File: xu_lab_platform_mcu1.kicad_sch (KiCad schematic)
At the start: 1 part, among them U1 STM32F446RCTx

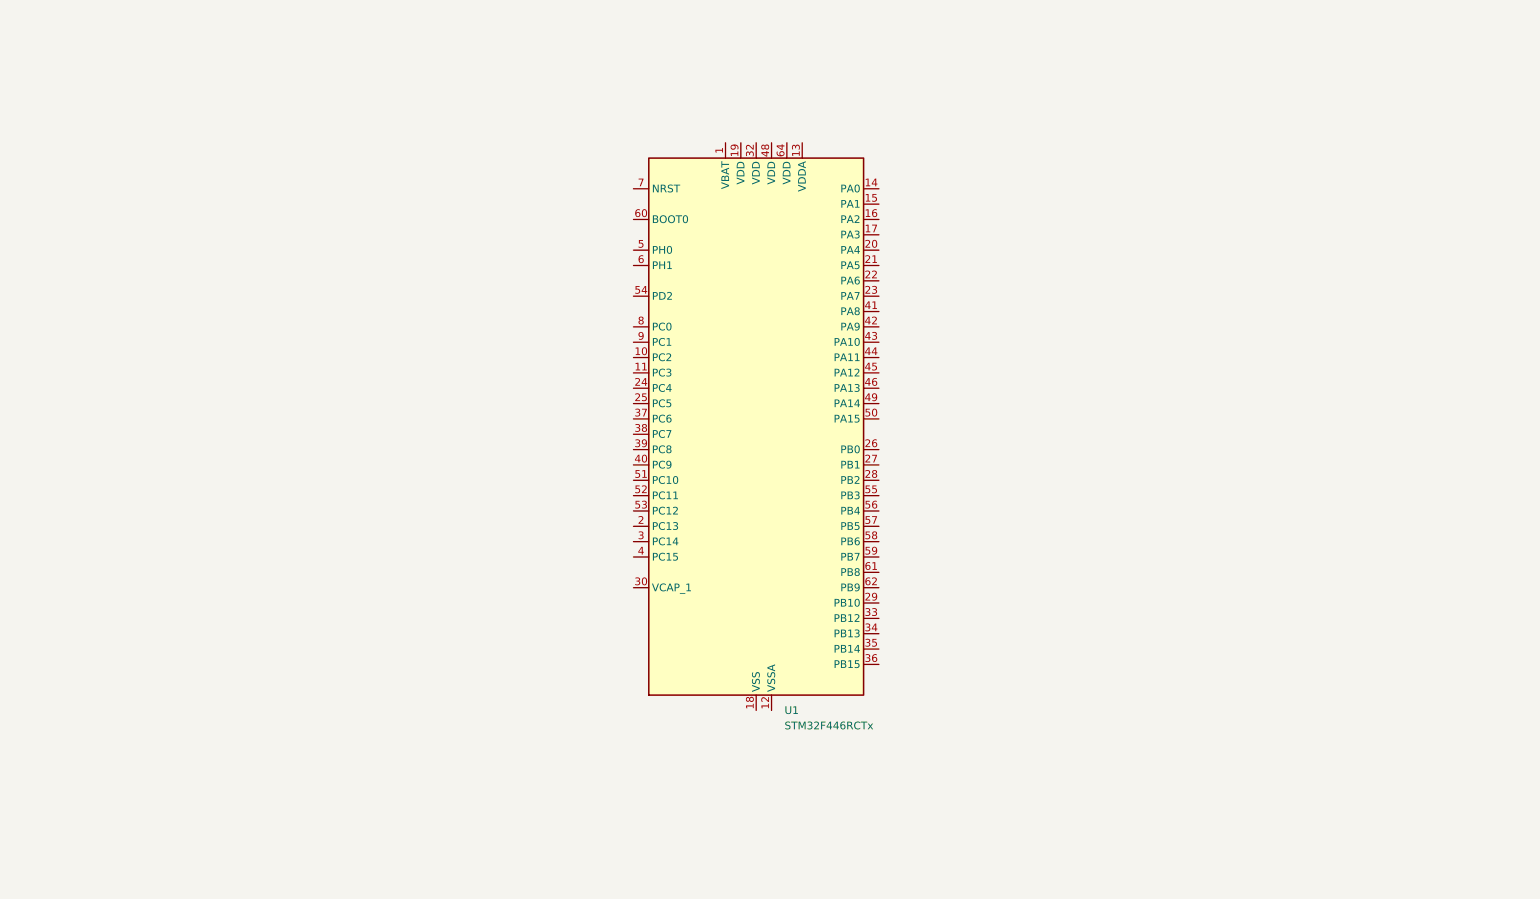
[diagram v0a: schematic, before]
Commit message: Connect power pins and add decoupling capacitors
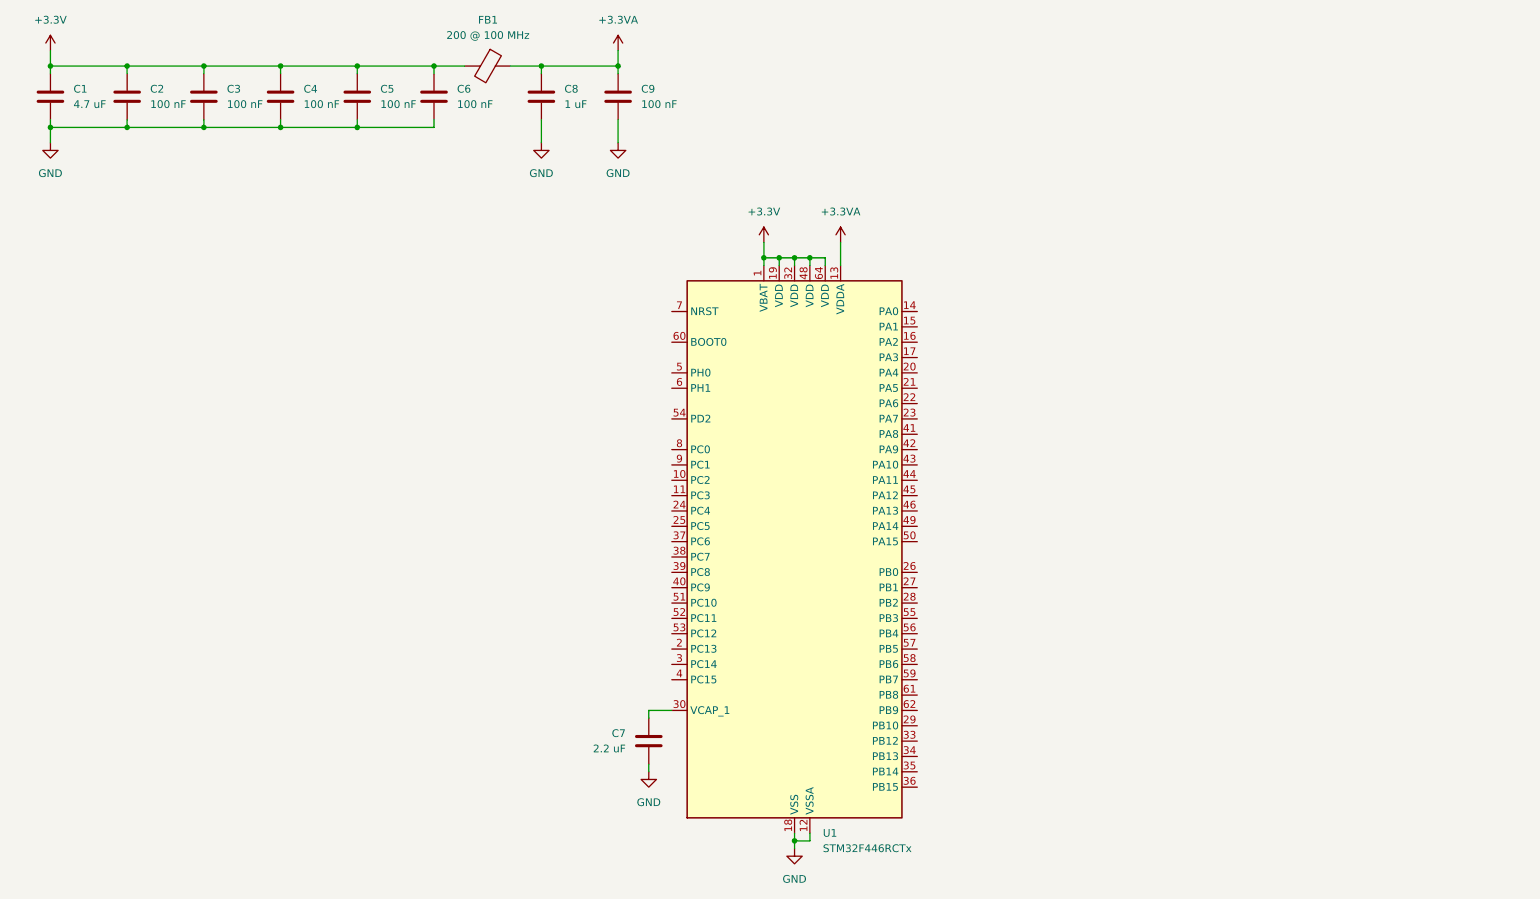
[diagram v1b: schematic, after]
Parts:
- added C1: 4.7 uF, symbol Device:C
- added C2, C3, C4, C5, C6, C9: 100 nF, symbol Device:C
- added C7: 2.2 uF, symbol Device:C
- added C8: 1 uF, symbol Device:C
- added FB1: 200 @ 100 MHz, symbol Device:FerriteBead
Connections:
- net +3.3V: now reaches U1.1 (VBAT)
- net +3.3V: now also U1.19 (VDD), U1.32 (VDD), U1.48 (VDD), U1.64 (VDD), C1.1, C2.1, C3.1, C4.1, C5.1, C6.1, FB1.2
- net GND: now reaches U1.12 (VSSA)
- net GND: now also U1.18 (VSS), U1.31 (VSS), U1.47 (VSS), U1.63 (VSS), C1.2, C2.2, C3.2, C4.2, C5.2, C6.2, C7.2, C8.2, C9.2
- net +3.3VA: now reaches U1.13 (VDDA)
- net +3.3VA: now also C8.1, C9.1, FB1.1
- net at U1.30 (VCAP_1): now also C7.1
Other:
- moved on the sheet: U1

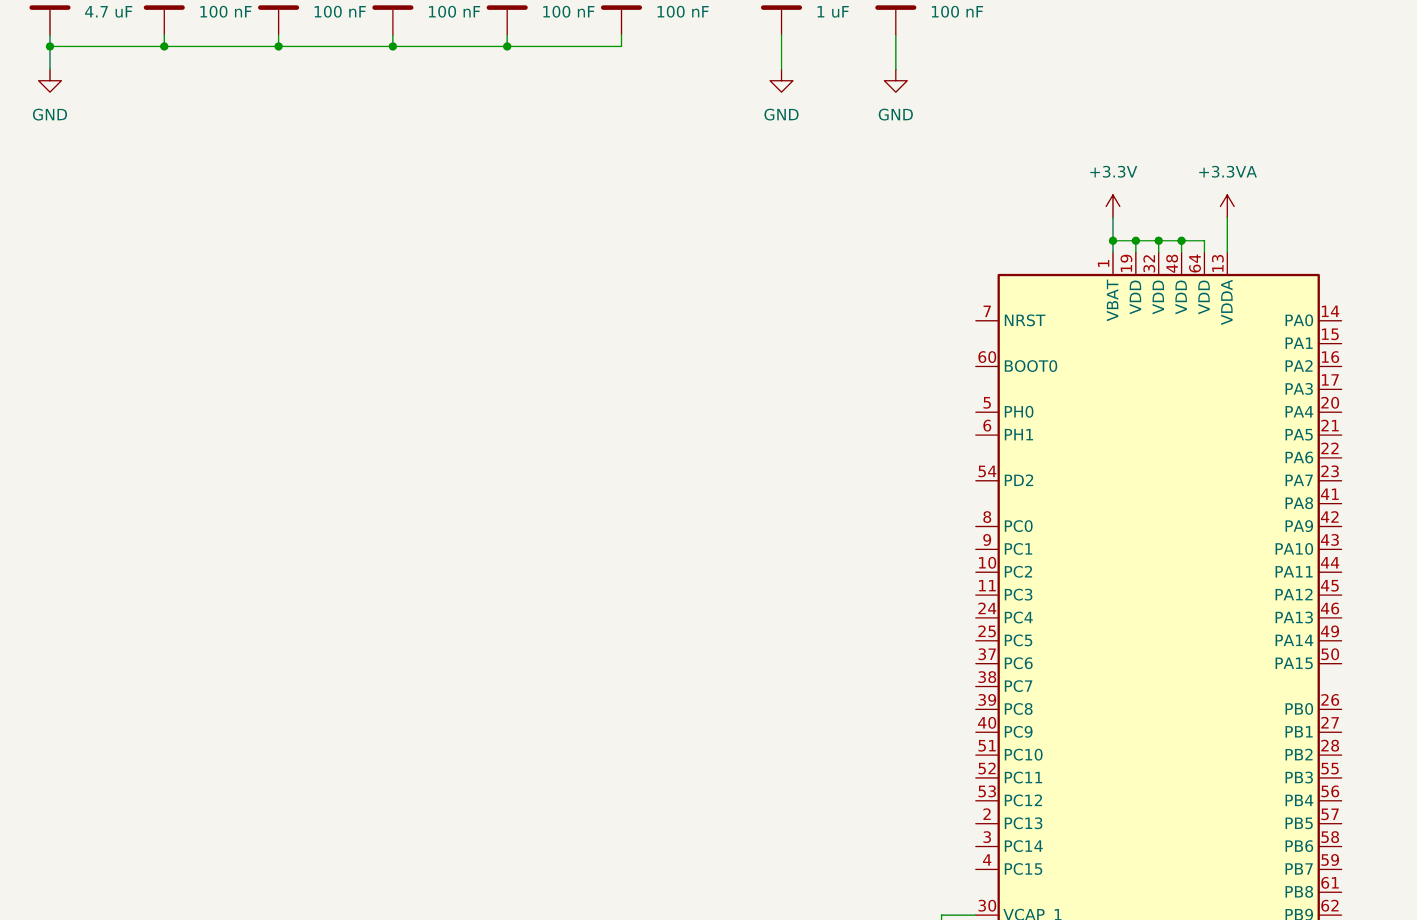
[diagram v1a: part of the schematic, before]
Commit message: Add circuits to configure reset and boot pins
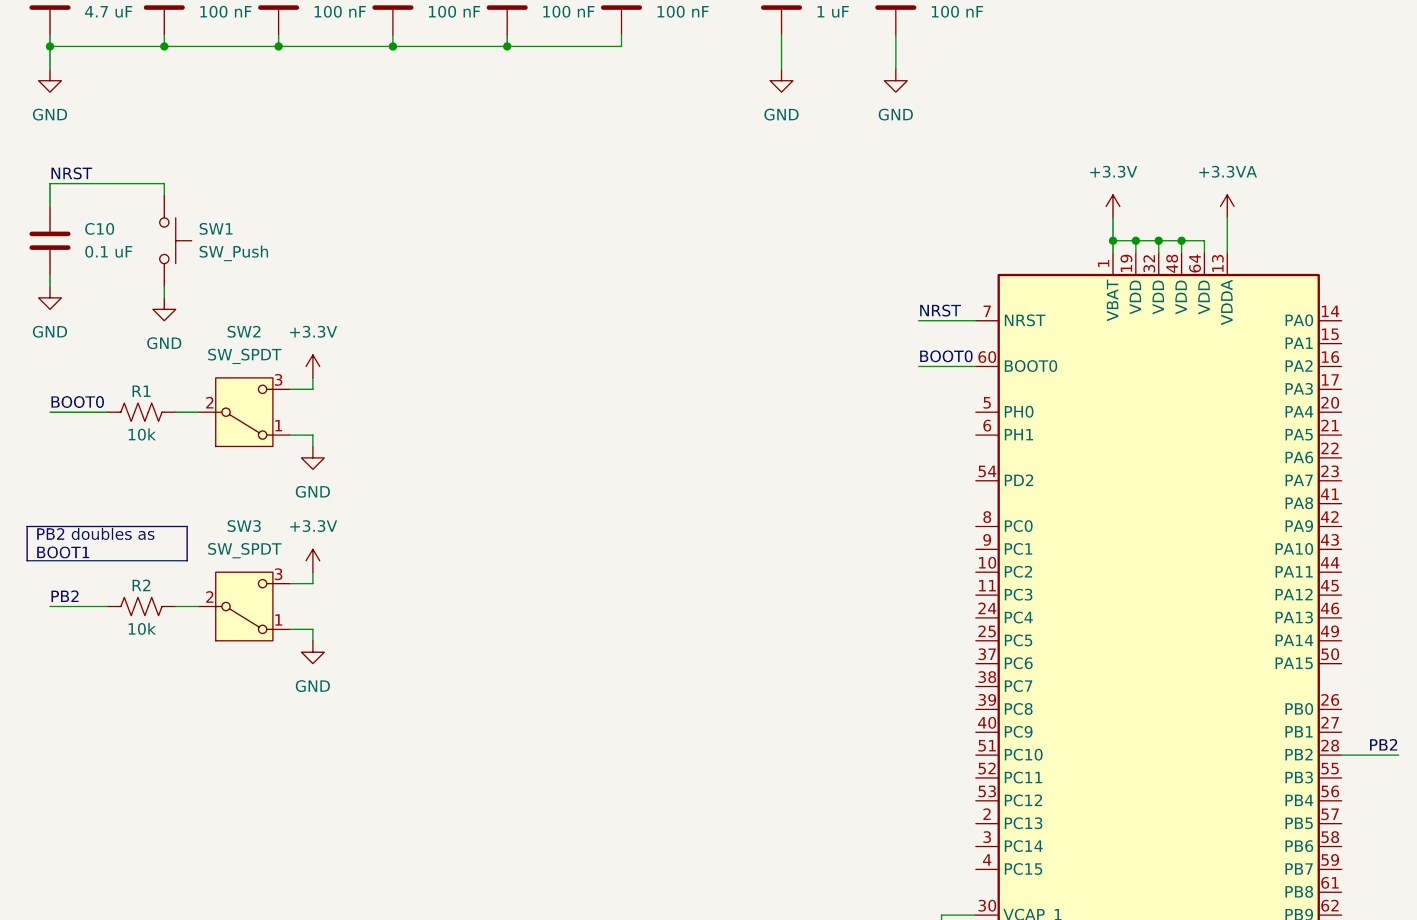
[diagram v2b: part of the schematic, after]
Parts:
- added C10: 0.1 uF, symbol Device:C
- added R1, R2: 10k, symbol Device:R_US
- added SW1: SW_Push, symbol Switch:SW_Push
- added SW2, SW3: SW_SPDT, symbol Switch:SW_SPDT
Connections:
- net +3.3V: now also SW2.3 (C), SW3.3 (C)
- net GND: now also C10.2, SW1.2, SW2.1 (A), SW3.1 (A)
- net PB2: now reaches U1.28 (PB2)
- net PB2: now also R2.2
- net BOOT0: now reaches U1.60 (BOOT0)
- net BOOT0: now also R1.2
- net NRST: now reaches U1.7 (NRST)
- net NRST: now also C10.1, SW1.1
- new net: R1.1, SW2.2 (B)
- new net: R2.1, SW3.2 (B)

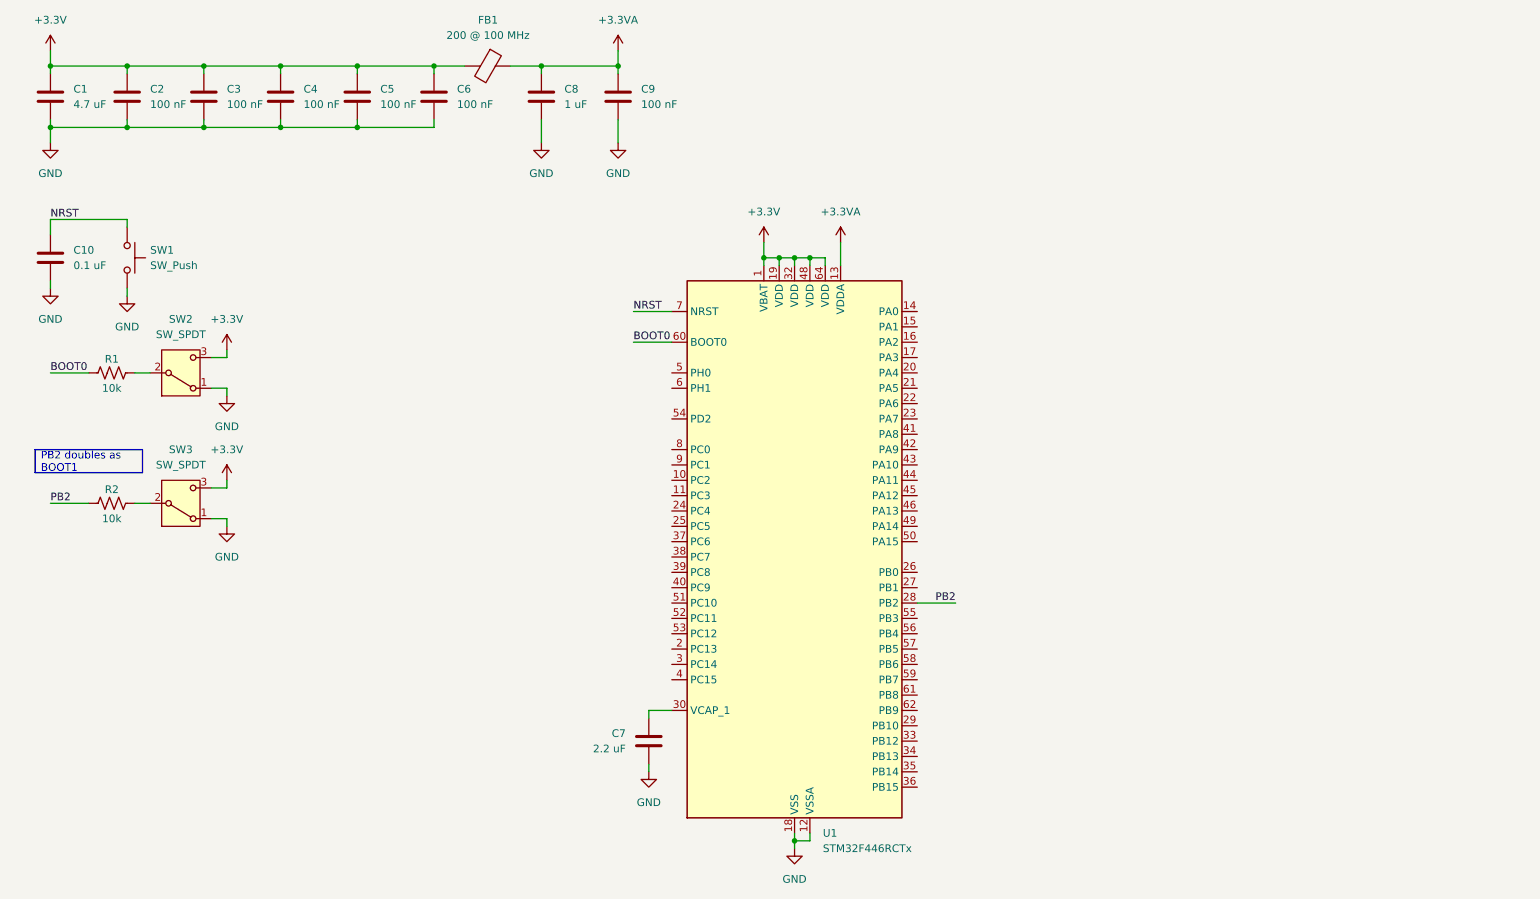
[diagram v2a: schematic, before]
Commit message: Add pin labels
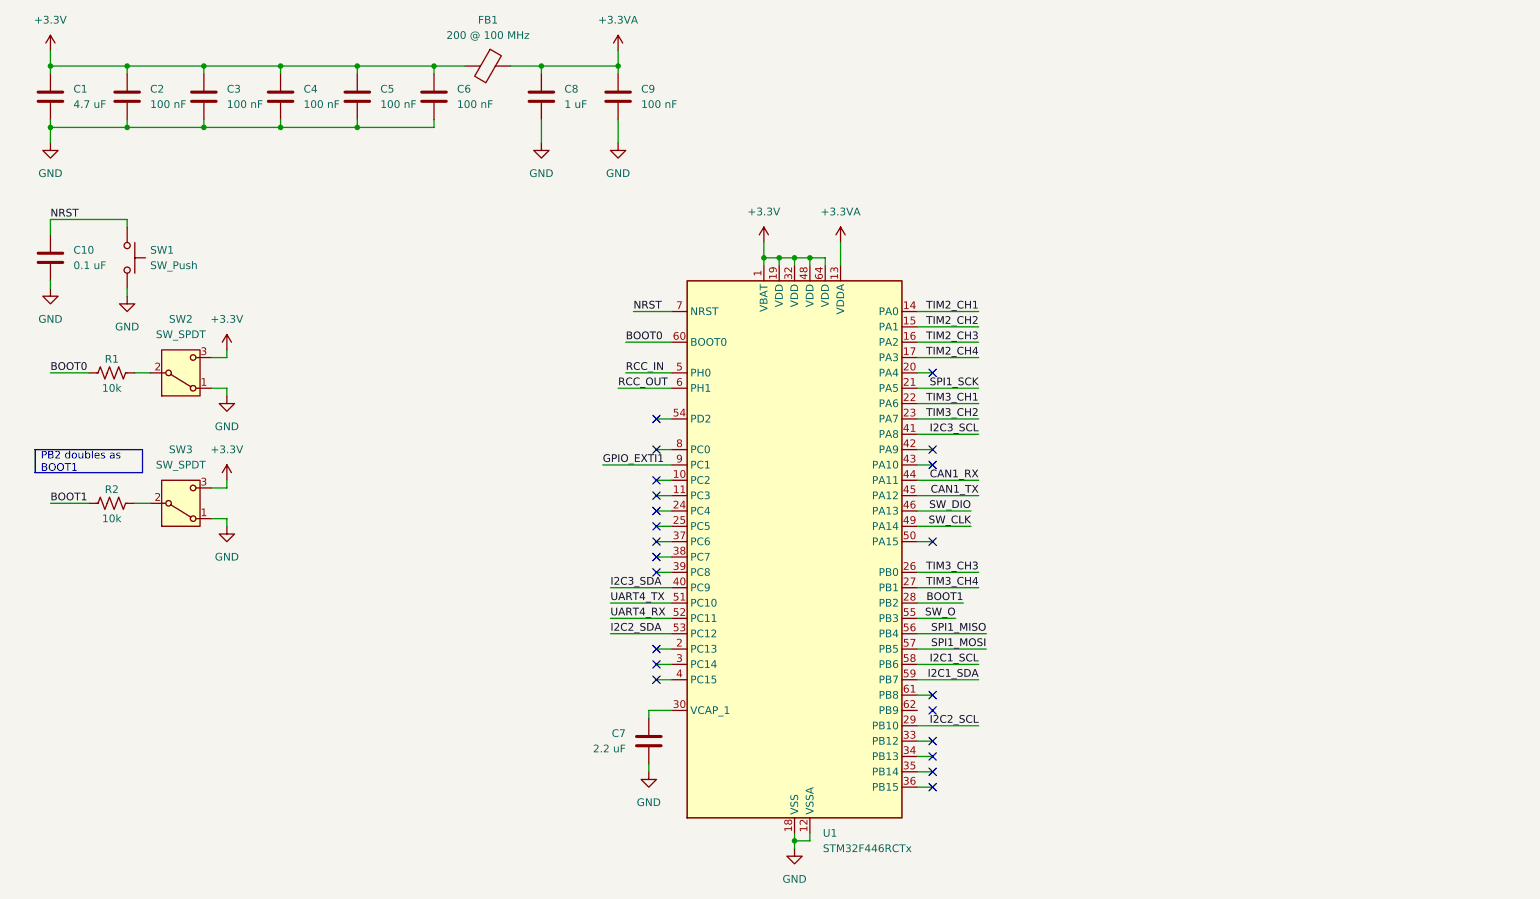
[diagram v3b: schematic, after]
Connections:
- net TIM2_CH1: now reaches U1.14 (PA0)
- net TIM2_CH2: now reaches U1.15 (PA1)
- net TIM2_CH3: now reaches U1.16 (PA2)
- net TIM2_CH4: now reaches U1.17 (PA3)
- net SPI1_SCK: now reaches U1.21 (PA5)
- net TIM3_CH1: now reaches U1.22 (PA6)
- net TIM3_CH2: now reaches U1.23 (PA7)
- net TIM3_CH3: now reaches U1.26 (PB0)
- net TIM3_CH4: now reaches U1.27 (PB1)
- net I2C2_SCL: now reaches U1.29 (PB10)
- net I2C3_SDA: now reaches U1.40 (PC9)
- net I2C3_SCL: now reaches U1.41 (PA8)
- net CAN1_RX: now reaches U1.44 (PA11)
- net CAN1_TX: now reaches U1.45 (PA12)
- net SW_DIO: now reaches U1.46 (PA13)
- net SW_CLK: now reaches U1.49 (PA14)
- net RCC_IN: now reaches U1.5 (PH0)
- net UART4_TX: now reaches U1.51 (PC10)
- net UART4_RX: now reaches U1.52 (PC11)
- net I2C2_SDA: now reaches U1.53 (PC12)
- net SW_O: now reaches U1.55 (PB3)
- net SPI1_MISO: now reaches U1.56 (PB4)
- net SPI1_MOSI: now reaches U1.57 (PB5)
- net I2C1_SCL: now reaches U1.58 (PB6)
- net I2C1_SDA: now reaches U1.59 (PB7)
- net RCC_OUT: now reaches U1.6 (PH1)
- net GPIO_EXTI1: now reaches U1.9 (PC1)
- net PB2 renamed BOOT1
- no-connect marks 0 -> 22

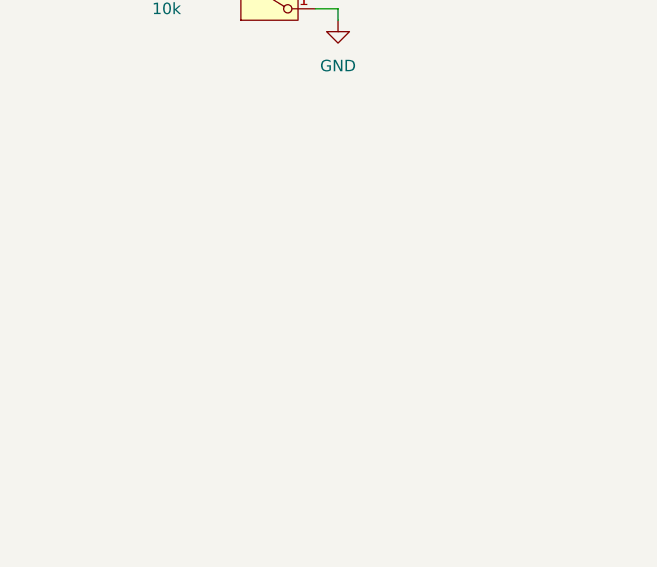
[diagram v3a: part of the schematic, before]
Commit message: Add external crystal oscillator
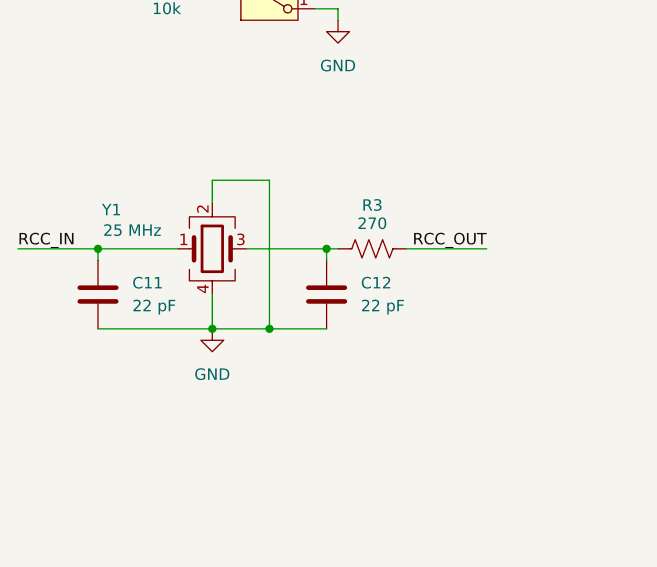
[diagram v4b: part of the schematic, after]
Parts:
- added C11, C12: 22 pF, symbol Device:C
- added R3: 270, symbol Device:R_US
- added Y1: 25 MHz, Crystal:Crystal_SMD_Abracon_ABM8G-4Pin_3.2x2.5mm, symbol Device:Crystal_GND24
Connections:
- net GND: now also C11.2, C12.2, Y1.2, Y1.4
- net RCC_IN: now also C11.1, Y1.1
- net RCC_OUT: now also R3.1
- new net: C12.1, R3.2, Y1.3

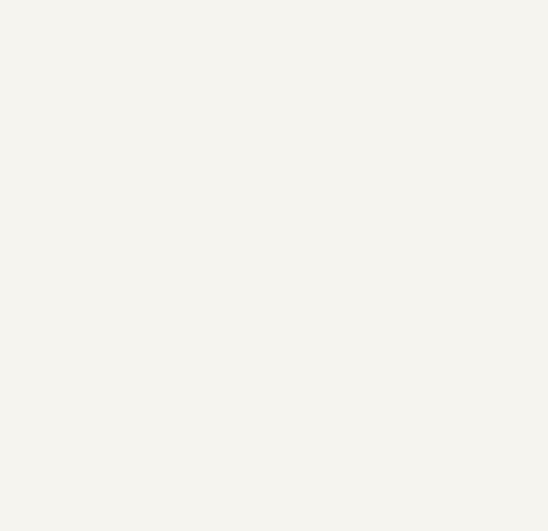
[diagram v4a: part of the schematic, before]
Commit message: Add SWD connections
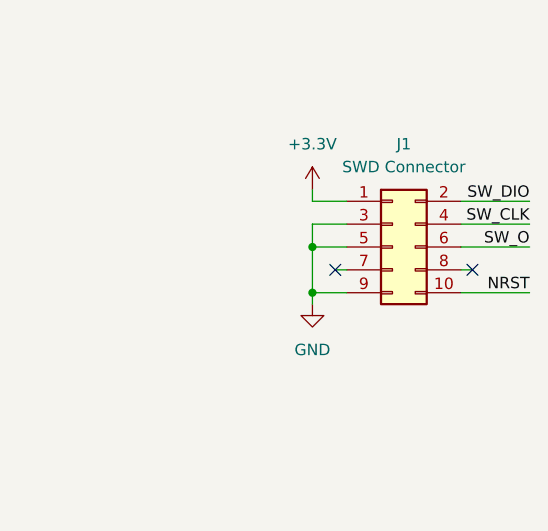
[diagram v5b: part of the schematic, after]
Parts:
- added J1: SWD Connector, symbol Connector_Generic:Conn_02x05_Odd_Even
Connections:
- net +3.3V: now also J1.1 (Pin_1)
- net GND: now also J1.3 (Pin_3), J1.5 (Pin_5), J1.9 (Pin_9)
- net NRST: now also J1.10 (Pin_10)
- net SW_CLK: now also J1.4 (Pin_4)
- net SW_DIO: now also J1.2 (Pin_2)
- net SW_O: now also J1.6 (Pin_6)
- no-connect marks 22 -> 24
